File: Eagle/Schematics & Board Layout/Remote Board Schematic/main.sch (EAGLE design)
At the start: 40 parts

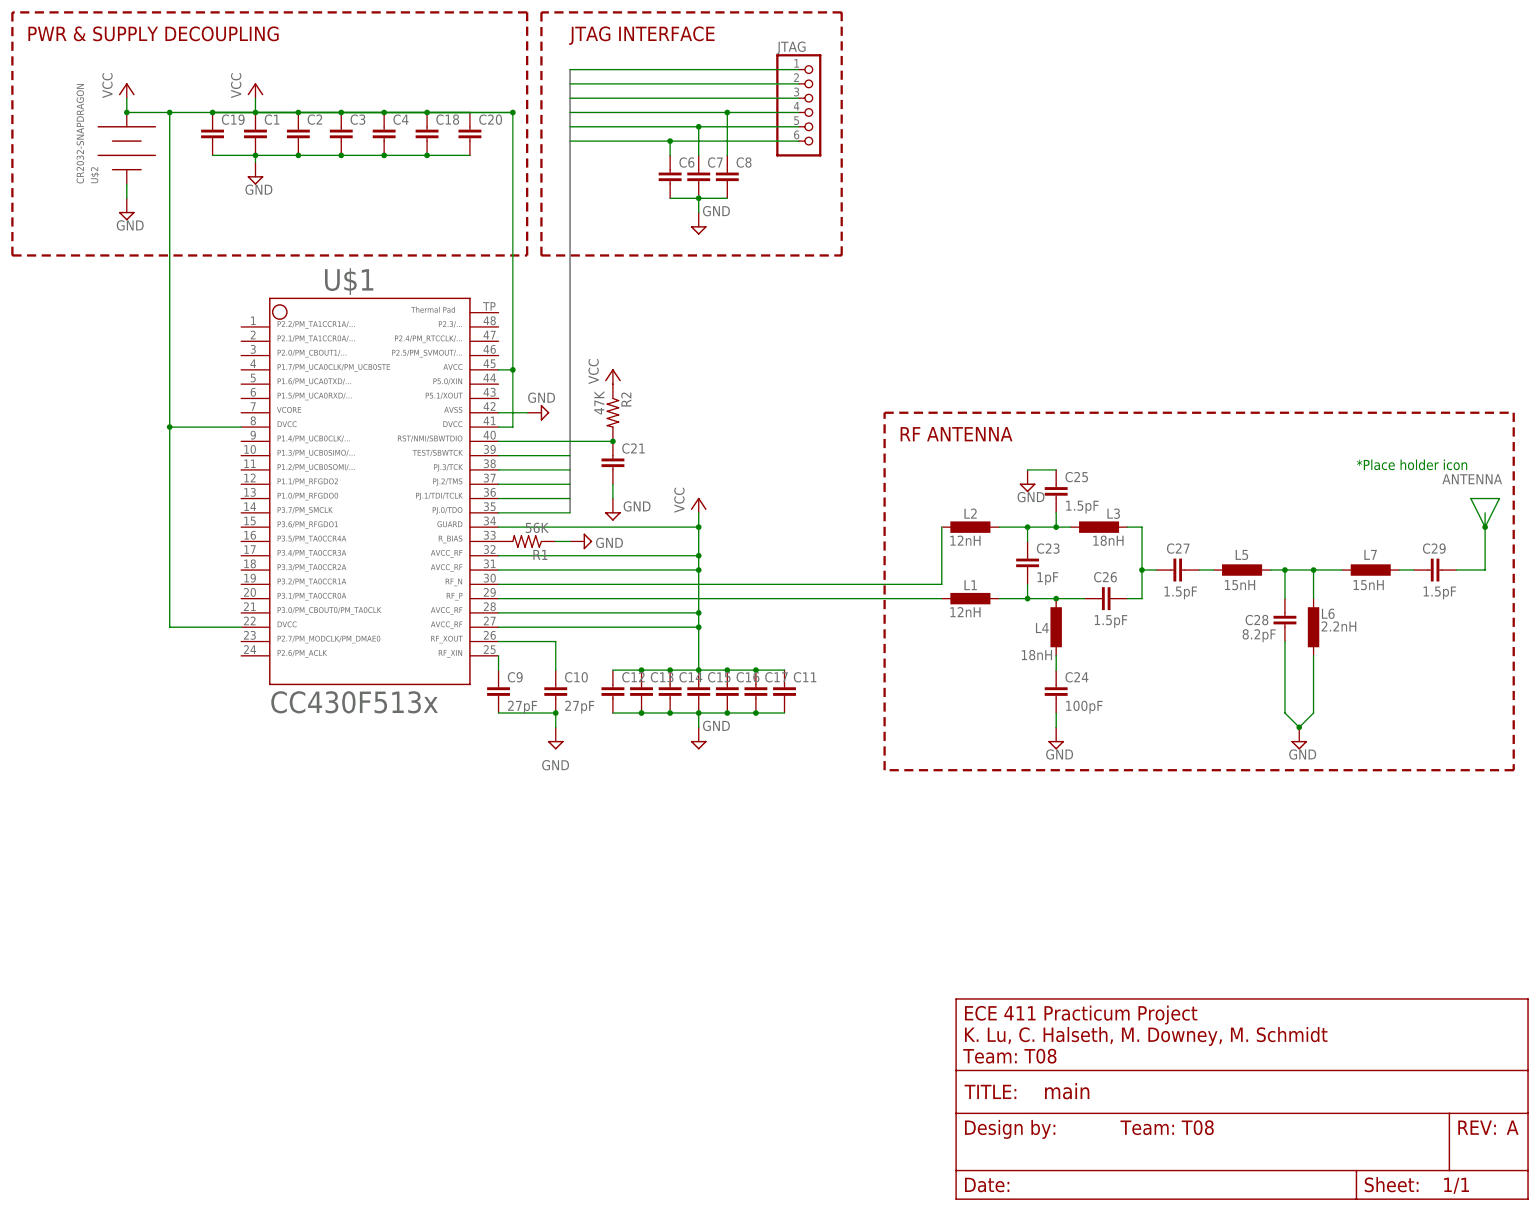
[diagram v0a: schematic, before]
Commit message: Revert "Schematic Update"
This reverts commit 5abb39e3185d2877969b4b6a32f7c4948c4e0dd3.
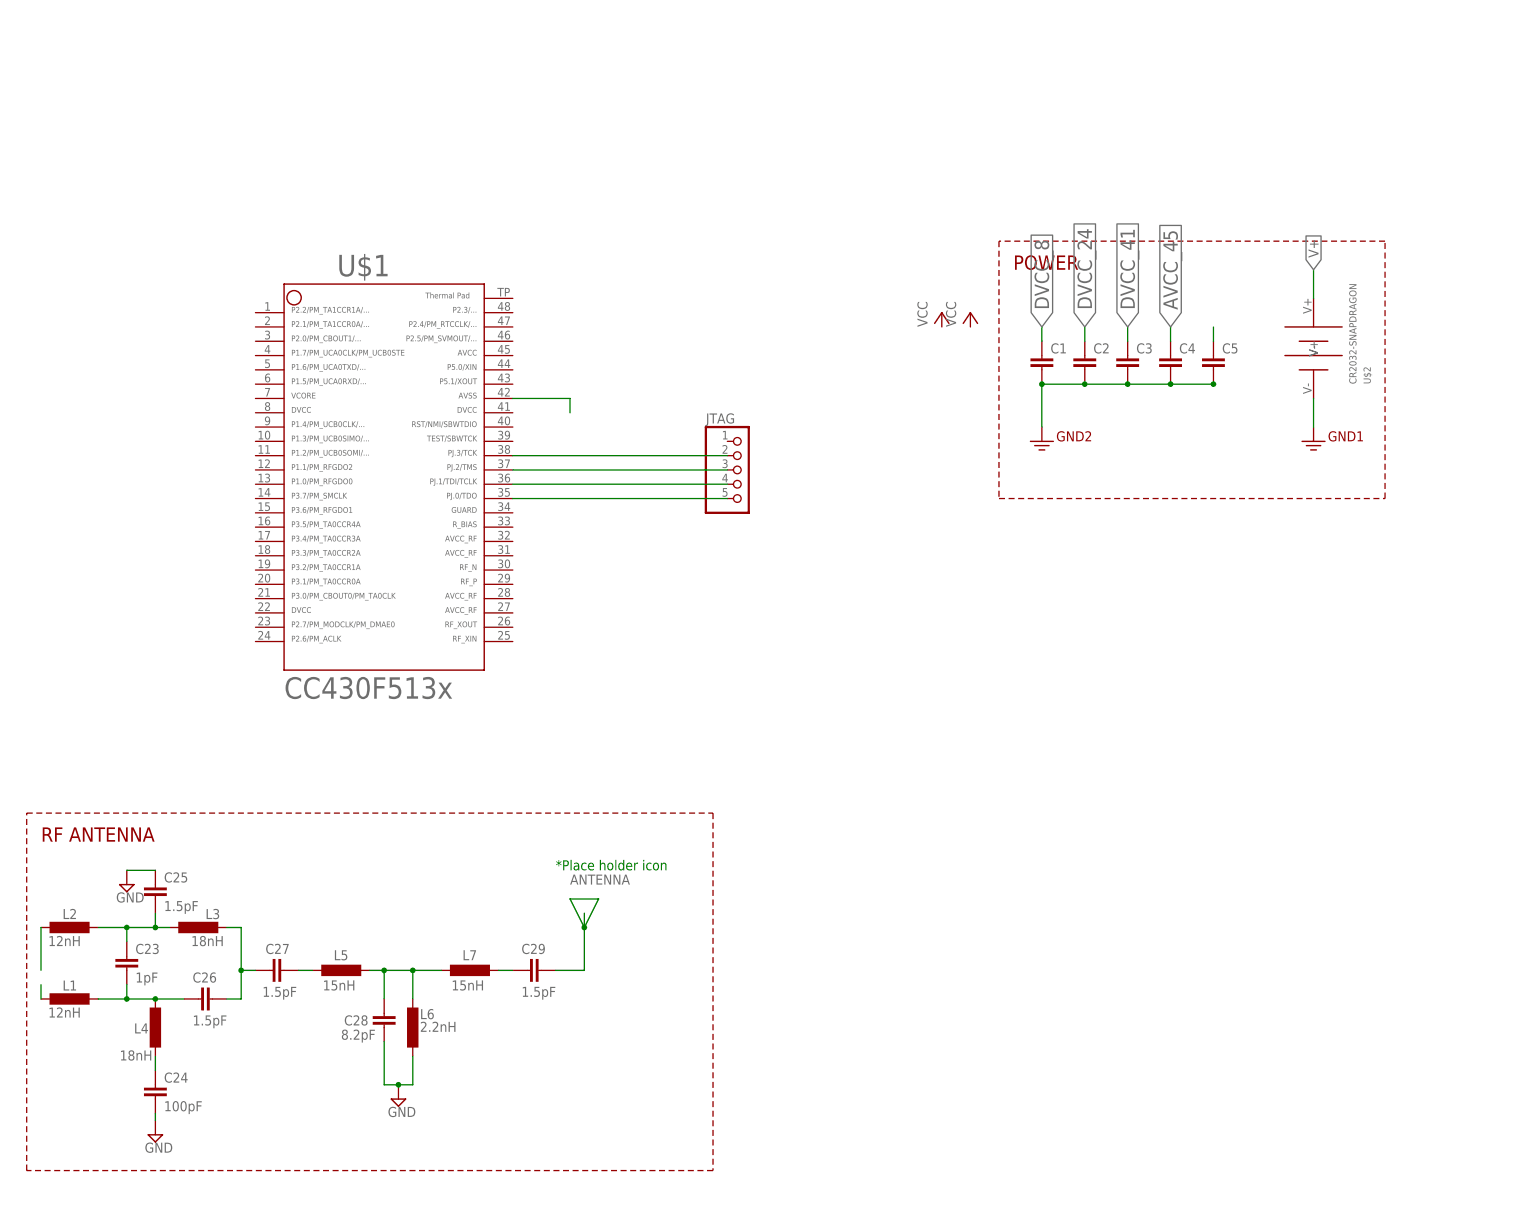
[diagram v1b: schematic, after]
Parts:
- removed C10, C9: 27pF, rcl:C-EUC0603
- removed C11, C12, C13, C14, C15, C16, C17, C18, C19, C20, C21, C6, C7, C8: (no value), rcl:C-EUC0603
- removed FRAME3: FRAME-LETTER, SparkFun-Aesthetics:FRAME-LETTER
- removed R1: 56K, rcl:R-US_R0603
- removed R2: 47K, rcl:R-US_R0603
- added C5: (no value), rcl:C-EUC0603
- JTAG: device adafruit:PINHD-1X6 -> aMJK_General:PINHD-1X5
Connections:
- removed net N$15: R1.2, U$1.33
- removed net SBWTCK: JTAG.2, U$1.39
- removed net SBWTDIO: C21.1, JTAG.1, R2.2, U$1.40
- removed net TCK: JTAG.3, U$1.38
- removed net TCLK: C7.1, JTAG.5, U$1.36
- removed net TDO: C6.1, JTAG.6, U$1.35
- removed net TMS: C8.1, JTAG.4, U$1.37
- removed net VCC: C1.1, C11.1, C12.1, C13.1, C14.1, C15.1, C16.1, C17.1, C18.1, C19.1, C2.1, C20.1, C3.1, C4.1, R2.1, U$1.22, U$1.27, U$1.28, U$1.31, U$1.32, U$1.34, U$1.41, U$1.45, U$1.8, U$2.V+
- new net 3.3V: C1.2, C2.2, C3.2, C4.2, C5.2
- new net AVCC_45: C4.1
- new net DVCC_24: C2.1
- new net DVCC_41: C3.1
- new net DVCC_8: C1.1
- new net N$11: JTAG.2, U$1.38
- new net N$12: JTAG.5, U$1.35
- new net N$13: JTAG.4, U$1.36
- new net N$7: JTAG.3, U$1.37
- new net V+: U$2.V+
- net GND: no longer C1.2, C10.2, C11.2, C12.2, C13.2, C14.2, C15.2, C16.2, C17.2, C18.2, C19.2, C2.2, C20.2, C21.2, C3.2, C4.2, C6.2, C7.2, C8.2, C9.2, R1.1, U$1.42
- net N$17: now also C5.1; no longer C10.1, U$1.26
- net N$9: now also U$1.42; no longer C9.1, U$1.25
- net RF_N: no longer U$1.30
- net RF_P: no longer U$1.29
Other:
- note added: "POWER"
- note removed: "A"
- note removed: "ECE 411 Practicum Project K. Lu, C. Halseth, M. Downey, M. Schmidt"
- note removed: "JTAG INTERFACE"
- note removed: "PWR & SUPPLY DECOUPLING"
- note removed: "Team: T08"
- moved on the sheet: C1, C2, C23, C24, C25, C26, C27, C28, C29, C3, C4, L1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

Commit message: Tx-Schematic Added
Additional eagle libraries; setup info added to datasheet section.
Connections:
- net 3.3V renamed N$10
- removed net AVCC_45: C4.1
- removed net DVCC_24: C2.1
- removed net DVCC_41: C3.1
- removed net DVCC_8: C1.1
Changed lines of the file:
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@@
 <setting verticaltext="up"/>
 </settings>
-<grid distance="0.1" unitdist="inch" unit="inch" style="lines" multiple="1" display="yes" altdistance="0.01" altunitdist="inch" altunit="inch"/>
+<grid distance="0.1" unitdist="inch" unit="inch" style="lines" multiple="1" display="no" altdistance="0.01" altunitdist="inch" altunit="inch"/>
 <layers>
 <layer number="1" name="Top" color="4" fill="1" visible="no" active="no"/>
@@
 <part name="SUPPLY3" library="supply2" deviceset="GND" device=""/>
 <part name="U$2" library="CR2032-SnapDragon" deviceset="CR2032-SNAPDRAGON" device=""/>
-<part name="GND1" library="SparkFun-Aesthetics" deviceset="GND2" device=""/>
 <part name="JTAG" library="aMJK_General" deviceset="PINHD-1X5" device=""/>
 <part name="C1" library="rcl" deviceset="C-EU" device="C0603"/>
@@
 <part name="C4" library="rcl" deviceset="C-EU" device="C0603"/>
 <part name="C5" library="rcl" deviceset="C-EU" device="C0603"/>
-<part name="GND2" library="SparkFun-Aesthetics" deviceset="GND2" device=""/>
-<part name="P+1" library="aVLA_SYmbols" deviceset="VCC" device=""/>
 <part name="P+2" library="aVLA_SYmbols" deviceset="VCC" device=""/>
 </parts>
@@
 <attribute name="NAME" x="246.38" y="144.78" size="1.27" layer="95" rot="R90"/>
 </instance>
-<instance part="GND1" gate="G$1" x="236.22" y="134.62"/>
 <instance part="JTAG" gate="A" x="134.62" y="129.54"/>
 <instance part="C1" gate="G$1" x="187.96" y="149.86"/>
@@
 <instance part="C4" gate="G$1" x="210.82" y="149.86"/>
 <instance part="C5" gate="G$1" x="218.44" y="149.86"/>
-<instance part="GND2" gate="G$1" x="187.96" y="134.62"/>
-<instance part="P+1" gate="VCC" x="170.18" y="157.48"/>
-<instance part="P+2" gate="VCC" x="175.26" y="157.48"/>
+<instance part="P+2" gate="VCC" x="187.96" y="157.48"/>
 </instances>
 <busses>
@@
 <pinref part="U$2" gate="G$1" pin="V-"/>
 <wire x1="236.22" y1="142.24" x2="236.22" y2="137.16" width="0.1524" layer="91"/>
-<pinref part="GND1" gate="G$1" pin="3.3V"/>
 </segment>
 </net>
@@
 </segment>
 </net>
-<net name="3.3V" class="0">
+<net name="N$17" class="0">
+<segment>
+<pinref part="C5" gate="G$1" pin="1"/>
+<wire x1="218.44" y1="152.4" x2="218.44" y2="154.94" width="0.1524" layer="91"/>
+</segment>
+</net>
+<net name="N$9" class="0">
+<segment>
+<pinref part="U$1" gate="G$1" pin="42"/>
+<wire x1="93.98" y1="142.24" x2="104.14" y2="142.24" width="0.1524" layer="91"/>
+<wire x1="104.14" y1="142.24" x2="104.14" y2="139.7" width="0.1524" layer="91"/>
+</segment>
+</net>
+<net name="N$10" class="0">
 <segment>
 <pinref part="C5" gate="G$1" pin="2"/>
@@
 <wire x1="195.58" y1="144.78" x2="187.96" y2="144.78" width="0.1524" layer="91"/>
 <wire x1="187.96" y1="144.78" x2="187.96" y2="137.16" width="0.1524" layer="91"/>
-<pinref part="GND2" gate="G$1" pin="3.3V"/>
 <pinref part="C1" gate="G$1" pin="2"/>
 <junction x="187.96" y="144.78"/>
@@
 </segment>
 </net>
-<net name="DVCC_8" class="0">
-<segment>
-<pinref part="C1" gate="G$1" pin="1"/>
-<wire x1="187.96" y1="152.4" x2="187.96" y2="154.94" width="0.1524" layer="91"/>
-<label x="187.96" y="154.94" size="2.54" layer="95" rot="R90" xref="yes"/>
-</segment>
-</net>
-<net name="DVCC_24" class="0">
-<segment>
-<pinref part="C2" gate="G$1" pin="1"/>
-<wire x1="195.58" y1="152.4" x2="195.58" y2="154.94" width="0.1524" layer="91"/>
-<label x="195.58" y="154.94" size="2.54" layer="95" rot="R90" xref="yes"/>
-</segment>
-</net>
-<net name="DVCC_41" class="0">
-<segment>
-<pinref part="C3" gate="G$1" pin="1"/>
-<wire x1="203.2" y1="152.4" x2="203.2" y2="154.94" width="0.1524" layer="91"/>
-<label x="203.2" y="154.94" size="2.54" layer="95" rot="R90" xref="yes"/>
-</segment>
-</net>
-<net name="AVCC_45" class="0">
-<segment>
-<pinref part="C4" gate="G$1" pin="1"/>
-<wire x1="210.82" y1="152.4" x2="210.82" y2="154.94" width="0.1524" layer="91"/>
-<label x="210.82" y="154.94" size="2.54" layer="95" rot="R90" xref="yes"/>
-</segment>
-</net>
-<net name="N$17" class="0">
-<segment>
-<pinref part="C5" gate="G$1" pin="1"/>
-<wire x1="218.44" y1="152.4" x2="218.44" y2="154.94" width="0.1524" layer="91"/>
-</segment>
-</net>
-<net name="N$9" class="0">
-<segment>
-<pinref part="U$1" gate="G$1" pin="42"/>
-<wire x1="93.98" y1="142.24" x2="104.14" y2="142.24" width="0.1524" layer="91"/>
-<wire x1="104.14" y1="142.24" x2="104.14" y2="139.7" width="0.1524" layer="91"/>
-</segment>
-</net>
